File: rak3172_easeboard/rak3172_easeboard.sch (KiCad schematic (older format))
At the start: 49 parts, among them J1 Conn_Coaxial, J2 USB_C_Receptacle_Simply, SW1 SW_Push, SW2 SW_Push, SW3 SW_Push, U1 RAK3172, U2 FT232RL, U3 SPX3819

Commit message: Matching Network
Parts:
- added C8_DNP1: DNP, rak3172_easeboard:C_0805_2012Metric_Pad1.18x1.45mm_HandSolder, symbol rak3172_easeboard:C
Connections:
- net GND: now also C8_DNP1.2
- net at J1.1 (In), R8.1: now also C8_DNP1.1
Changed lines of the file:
@@
 L rak3172_easeboard:GND #PWR03
 U 1 1 61AD1456
-P 1150 6950
-F 0 "#PWR03" H 1150 6700 50  0001 C CNN
-F 1 "GND" H 1155 6777 50  0000 C CNN
-F 2 "" H 1150 6950 50  0001 C CNN
-F 3 "" H 1150 6950 50  0001 C CNN
-	1    1150 6950
-	1    0    0    -1
-$EndComp
-Wire Wire Line
-	1900 6600 1900 6950
-Wire Wire Line
-	1150 6950 1150 6900
+P 1150 7250
+F 0 "#PWR03" H 1150 7000 50  0001 C CNN
+F 1 "GND" H 1155 7077 50  0000 C CNN
+F 2 "" H 1150 7250 50  0001 C CNN
+F 3 "" H 1150 7250 50  0001 C CNN
+	1    1150 7250
+	1    0    0    -1
+$EndComp
 $Comp
 L rak3172_easeboard:VCC #PWR013
@@
 L rak3172_easeboard:GND #PWR04
 U 1 1 6153D503
-P 1900 6950
-F 0 "#PWR04" H 1900 6700 50  0001 C CNN
-F 1 "GND" H 1905 6777 50  0000 C CNN
-F 2 "" H 1900 6950 50  0001 C CNN
-F 3 "" H 1900 6950 50  0001 C CNN
-	1    1900 6950
+P 1900 7250
+F 0 "#PWR04" H 1900 7000 50  0001 C CNN
+F 1 "GND" H 1905 7077 50  0000 C CNN
+F 2 "" H 1900 7250 50  0001 C CNN
+F 3 "" H 1900 7250 50  0001 C CNN
+	1    1900 7250
 	1    0    0    -1
 $EndComp
@@
 	1800 6700 2050 6700
 Wire Wire Line
-	1500 6700 1350 6700
+	1500 6700 1400 6700
 Text Notes 2700 700  0    100  ~ 20
 USB-SERIAL CONVERTER
@@
 Wire Wire Line
 	4500 6000 4650 6000
+$Comp
+L rak3172_easeboard:C C8_DNP1
+U 1 1 61CCCB7A
+P 1400 6950
+F 0 "C8_DNP1" H 1515 6996 50  0000 L CNN
+F 1 "DNP" H 1515 6905 50  0000 L CNN
+F 2 "rak3172_easeboard:C_0805_2012Metric_Pad1.18x1.45mm_HandSolder" H 1350 6450 50  0001 C CNN
+F 3 "https://www.mouser.es/datasheet/2/212/KEM_C1002_X7R_SMD-1102033.pdf" H 1400 6950 50  0001 C CNN
+F 4 "0.09" H 1400 6950 50  0001 C CNN "Last Seen Price (eur)"
+F 5 "https://www.mouser.es/ProductDetail/KEMET/C0805C104M5RACTU?qs=sGAEpiMZZMsh%252B1woXyUXj%252BSRFd9RE8bC9ywBatmv%2F3c%3D" H 1400 6950 50  0001 C CNN "Mouser"
+	1    1400 6950
+	1    0    0    -1
+$EndComp
+$Comp
+L rak3172_easeboard:GND #PWR034
+U 1 1 61CFA2AD
+P 1400 7250
+F 0 "#PWR034" H 1400 7000 50  0001 C CNN
+F 1 "GND" H 1405 7077 50  0000 C CNN
+F 2 "" H 1400 7250 50  0001 C CNN
+F 3 "" H 1400 7250 50  0001 C CNN
+	1    1400 7250
+	1    0    0    -1
+$EndComp
+Wire Wire Line
+	1150 6900 1150 7250
+Wire Wire Line
+	1400 7100 1400 7250
+Wire Wire Line
+	1900 6600 1900 7250
+Wire Wire Line
+	1400 6800 1400 6700
+Connection ~ 1400 6700
+Wire Wire Line
+	1400 6700 1350 6700
 $EndSCHEMATC

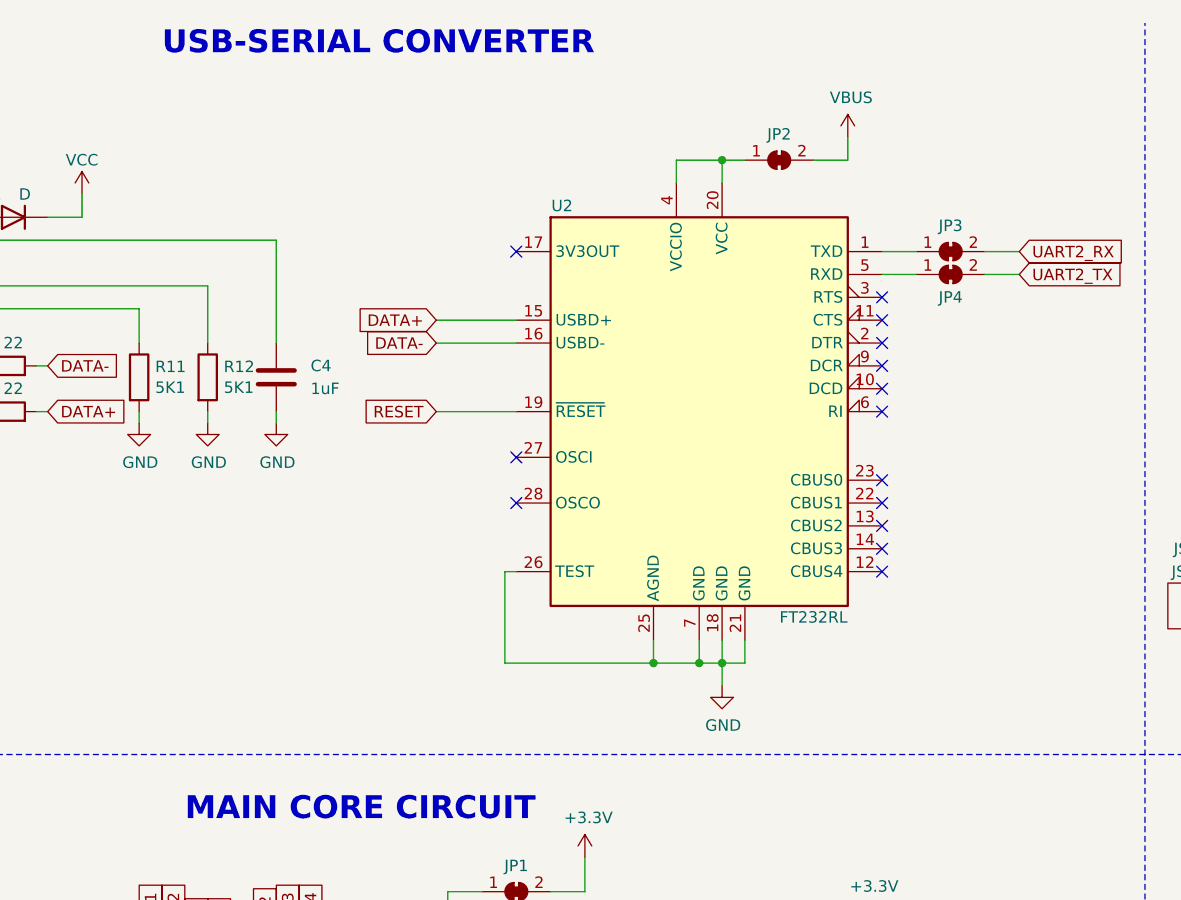
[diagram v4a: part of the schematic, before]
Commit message: Disconnect Reset from usb-serial converter
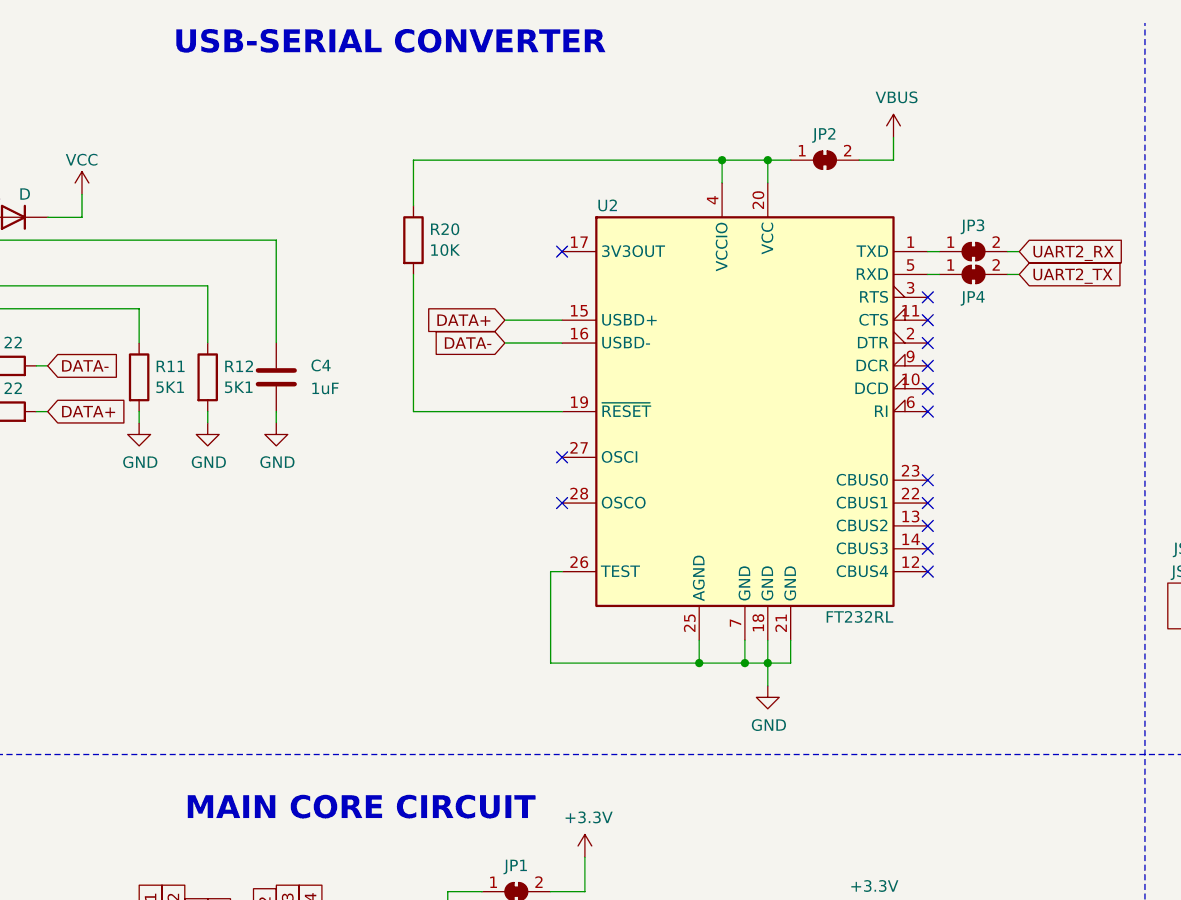
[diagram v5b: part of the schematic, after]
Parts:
- added R20: 10K, rak3172_easeboard:R_0805_2012Metric_Pad1.20x1.40mm_HandSolder, symbol rak3172_easeboard:R
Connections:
- net RESET: no longer U2.19 (~RESET~)
- net at JP2.1 (A), U2.20 (VCC), U2.4 (VCCIO): now also R20.1
- new net: R20.2, U2.19 (~RESET~)
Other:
- moved on the sheet: JP2, JP3, JP4, U2
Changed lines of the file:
@@
 L rak3172_easeboard:GND #PWR010
 U 1 1 61DF3F73
-P 5150 3450
-F 0 "#PWR010" H 5150 3200 50  0001 C CNN
-F 1 "GND" H 5155 3277 50  0000 C CNN
-F 2 "" H 5150 3450 50  0001 C CNN
-F 3 "" H 5150 3450 50  0001 C CNN
-	1    5150 3450
-	1    0    0    -1
-$EndComp
-Wire Wire Line
-	5150 3250 5150 3350
+P 5350 3450
+F 0 "#PWR010" H 5350 3200 50  0001 C CNN
+F 1 "GND" H 5355 3277 50  0000 C CNN
+F 2 "" H 5350 3450 50  0001 C CNN
+F 3 "" H 5350 3450 50  0001 C CNN
+	1    5350 3450
+	1    0    0    -1
+$EndComp
+Wire Wire Line
+	5350 3250 5350 3350
+Wire Wire Line
+	5450 3250 5450 3350
+Wire Wire Line
+	5450 3350 5350 3350
+Connection ~ 5350 3350
+Wire Wire Line
+	5350 3350 5350 3450
 Wire Wire Line
 	5250 3250 5250 3350
 Wire Wire Line
-	5250 3350 5150 3350
-Connection ~ 5150 3350
-Wire Wire Line
-	5150 3350 5150 3450
+	5250 3350 5350 3350
+Text GLabel 4200 1850 0    50   Input ~ 0
+DATA+
+Text GLabel 4200 1950 0    50   Input ~ 0
+DATA-
 Wire Wire Line
 	5050 3250 5050 3350
 Wire Wire Line
-	5050 3350 5150 3350
-Text GLabel 3900 1850 0    50   Input ~ 0
-DATA+
-Text GLabel 3900 1950 0    50   Input ~ 0
-DATA-
-Wire Wire Line
-	3900 1950 4250 1950
-Wire Wire Line
-	4250 1850 3900 1850
-Wire Wire Line
-	4850 3250 4850 3350
-Wire Wire Line
-	4850 3350 5050 3350
+	5050 3350 5250 3350
+Connection ~ 5250 3350
+Wire Wire Line
+	4450 2950 4400 2950
+Wire Wire Line
+	4400 2950 4400 3350
+Wire Wire Line
+	4400 3350 5050 3350
 Connection ~ 5050 3350
-Wire Wire Line
-	4250 2950 4200 2950
-Wire Wire Line
-	4200 2950 4200 3350
-Wire Wire Line
-	4200 3350 4850 3350
-Connection ~ 4850 3350
 $Comp
 L rak3172_easeboard:FT232RL U2
 U 1 1 61DF0F84
-P 5050 2250
-F 0 "U2" H 4450 3150 50  0000 C CNN
-F 1 "FT232RL" H 5550 1350 50  0000 C CNN
-F 2 "rak3172_easeboard:SSOP-28_5.3x10.2mm_P0.65mm" H 6150 1350 50  0001 C CNN
-F 3 "https://www.ftdichip.com/Support/Documents/DataSheets/ICs/DS_FT232R.pdf" H 5050 2250 50  0001 C CNN
-	1    5050 2250
-	1    0    0    -1
-$EndComp
-Wire Wire Line
-	4950 1150 4950 1250
-Wire Wire Line
-	5150 1250 5150 1150
-Connection ~ 5150 1150
-Wire Wire Line
-	5150 1150 4950 1150
-Text GLabel 6450 1550 2    50   Input ~ 0
-UART2_RX
-Text GLabel 6450 1650 2    50   Input ~ 0
-UART2_TX
+P 5250 2250
+F 0 "U2" H 4650 3150 50  0000 C CNN
+F 1 "FT232RL" H 5750 1350 50  0000 C CNN
+F 2 "rak3172_easeboard:SSOP-28_5.3x10.2mm_P0.65mm" H 6350 1350 50  0001 C CNN
+F 3 "https://www.ftdichip.com/Support/Documents/DataSheets/ICs/DS_FT232R.pdf" H 5250 2250 50  0001 C CNN
+	1    5250 2250
+	1    0    0    -1
+$EndComp
+Wire Wire Line
+	5150 1150 5150 1250
+Wire Wire Line
+	5350 1250 5350 1150
+Connection ~ 5350 1150
+Wire Wire Line
+	5350 1150 5150 1150
 Wire Wire Line
 	3150 7250 3150 6950
@@
 Wire Wire Line
 	1500 6700 1400 6700
-Text Notes 2700 700  0    100  ~ 20
+Text Notes 2750 700  0    100  ~ 20
 USB-SERIAL CONVERTER
 $Comp
@@
 Battery Connector
 Wire Wire Line
-	5150 1150 5250 1150
+	5350 1150 5450 1150
 Wire Wire Line
 	3950 4350 4100 4350
@@
 L rak3172_easeboard:SolderJumper_2_Bridged JP2
 U 1 1 61BC7834
-P 5400 1150
-F 0 "JP2" H 5400 1263 50  0000 C CNN
-F 1 "SolderJumper_2_Bridged" H 5400 1050 50  0001 C CNN
-F 2 "rak3172_easeboard:SolderJumper-2_P1.3mm_Bridged_Pad1.0x1.5mm" H 5400 1150 50  0001 C CNN
-F 3 "~" H 5400 1150 50  0001 C CNN
-F 4 "~" H 5400 1150 50  0001 C CNN "Last Seen Price (eur)"
-	1    5400 1150
+P 5600 1150
+F 0 "JP2" H 5600 1263 50  0000 C CNN
+F 1 "SolderJumper_2_Bridged" H 5600 1050 50  0001 C CNN
+F 2 "rak3172_easeboard:SolderJumper-2_P1.3mm_Bridged_Pad1.0x1.5mm" H 5600 1150 50  0001 C CNN
+F 3 "~" H 5600 1150 50  0001 C CNN
+F 4 "~" H 5600 1150 50  0001 C CNN "Last Seen Price (eur)"
+	1    5600 1150
 	1    0    0    -1
 $EndComp
@@
 L rak3172_easeboard:VBUS #PWR025
 U 1 1 6176782E
-P 5700 1050
-F 0 "#PWR025" H 5700 900 50  0001 C CNN
-F 1 "VBUS" H 5715 1223 50  0000 C CNN
-F 2 "" H 5700 1050 50  0001 C CNN
-F 3 "" H 5700 1050 50  0001 C CNN
-	1    5700 1050
-	1    0    0    -1
-$EndComp
-NoConn ~ 5850 2550
-NoConn ~ 5850 2650
-NoConn ~ 5850 2750
-NoConn ~ 5850 2850
-NoConn ~ 5850 2950
-NoConn ~ 5850 2250
-NoConn ~ 5850 2150
-NoConn ~ 4250 2650
-NoConn ~ 4250 2450
-NoConn ~ 5850 2050
-NoConn ~ 5850 1950
-NoConn ~ 5850 1850
-NoConn ~ 5850 1750
-NoConn ~ 4250 1550
-Text GLabel 3900 2250 0    50   Input ~ 0
-RESET
+P 5900 1050
+F 0 "#PWR025" H 5900 900 50  0001 C CNN
+F 1 "VBUS" H 5915 1223 50  0000 C CNN
+F 2 "" H 5900 1050 50  0001 C CNN
+F 3 "" H 5900 1050 50  0001 C CNN
+	1    5900 1050
+	1    0    0    -1
+$EndComp
+NoConn ~ 6050 2550
+NoConn ~ 6050 2650
+NoConn ~ 6050 2750
+NoConn ~ 6050 2850
+NoConn ~ 6050 2950
+NoConn ~ 6050 2250
+NoConn ~ 6050 2150
+NoConn ~ 4450 2650
+NoConn ~ 4450 2450
+NoConn ~ 6050 2050
+NoConn ~ 6050 1950
+NoConn ~ 6050 1850
+NoConn ~ 6050 1750
+NoConn ~ 4450 1550
 $Comp
 L rak3172_easeboard:R R2
@@
 $EndComp
 Wire Wire Line
-	4250 2250 3900 2250
-Wire Wire Line
 	8900 2000 8900 2050
 Wire Wire Line
@@
 	8200 2900 8200 2950
 Wire Wire Line
-	5700 1050 5700 1150
-Wire Wire Line
-	5700 1150 5550 1150
+	5900 1050 5900 1150
+Wire Wire Line
+	5900 1150 5750 1150
 Wire Wire Line
 	850  4950 1050 4950
@@
 $EndComp
 Wire Wire Line
-	6300 1650 6450 1650
-Wire Wire Line
-	5850 1650 6000 1650
-Wire Wire Line
-	6300 1550 6450 1550
-Wire Wire Line
-	5850 1550 6000 1550
-$Comp
-L rak3172_easeboard:SolderJumper_2_Bridged JP4
-U 1 1 61BC86E2
-P 6150 1650
-F 0 "JP4" H 6150 1550 50  0000 C CNN
-F 1 "SolderJumper_2_Bridged" H 6150 1550 50  0001 C CNN
-F 2 "rak3172_easeboard:SolderJumper-2_P1.3mm_Bridged_Pad1.0x1.5mm" H 6150 1650 50  0001 C CNN
-F 3 "~" H 6150 1650 50  0001 C CNN
-F 4 "~" H 6150 1650 50  0001 C CNN "Last Seen Price (eur)"
-	1    6150 1650
-	1    0    0    -1
-$EndComp
-$Comp
-L rak3172_easeboard:SolderJumper_2_Bridged JP3
-U 1 1 61BC80B7
-P 6150 1550
-F 0 "JP3" H 6150 1663 50  0000 C CNN
-F 1 "SolderJumper_2_Bridged" H 6150 1450 50  0001 C CNN
-F 2 "rak3172_easeboard:SolderJumper-2_P1.3mm_Bridged_Pad1.0x1.5mm" H 6150 1550 50  0001 C CNN
-F 3 "~" H 6150 1550 50  0001 C CNN
-F 4 "~" H 6150 1550 50  0001 C CNN "Last Seen Price (eur)"
-	1    6150 1550
-	1    0    0    -1
-$EndComp
-Wire Wire Line
 	1750 5000 1750 4950
 Wire Wire Line
@@
 Wire Wire Line
 	1400 6700 1350 6700
+$Comp
+L rak3172_easeboard:R R20
+U 1 1 627371A7
+P 3800 1500
+F 0 "R20" H 3870 1546 50  0000 L CNN
+F 1 "10K" H 3870 1455 50  0000 L CNN
+F 2 "rak3172_easeboard:R_0805_2012Metric_Pad1.20x1.40mm_HandSolder" V 3730 1500 50  0001 C CNN
+F 3 "https://www.mouser.es/datasheet/2/392/susumu_RR_Data_Sheet-1206438.pdf" H 3800 1500 50  0001 C CNN
+F 4 "0.09" H 3800 1500 50  0001 C CNN "Last Seen Price (eur)"
+F 5 "https://www.mouser.es/ProductDetail/Susumu/RR1220P-103-D?qs=nCAm%252BcMdy9wM6YRNq%2FvwoQ%3D%3D" H 3800 1500 50  0001 C CNN "Mouser"
+	1    3800 1500
+	1    0    0    -1
+$EndComp
+$Comp
+L rak3172_easeboard:SolderJumper_2_Bridged JP3
+U 1 1 61BC80B7
+P 6250 1550
+F 0 "JP3" H 6250 1663 50  0000 C CNN
+F 1 "SolderJumper_2_Bridged" H 6250 1450 50  0001 C CNN
+F 2 "rak3172_easeboard:SolderJumper-2_P1.3mm_Bridged_Pad1.0x1.5mm" H 6250 1550 50  0001 C CNN
+F 3 "~" H 6250 1550 50  0001 C CNN
+F 4 "~" H 6250 1550 50  0001 C CNN "Last Seen Price (eur)"
+	1    6250 1550
+	1    0    0    -1
+$EndComp
+$Comp
+L rak3172_easeboard:SolderJumper_2_Bridged JP4
+U 1 1 61BC86E2
+P 6250 1650
+F 0 "JP4" H 6250 1550 50  0000 C CNN
+F 1 "SolderJumper_2_Bridged" H 6250 1550 50  0001 C CNN
+F 2 "rak3172_easeboard:SolderJumper-2_P1.3mm_Bridged_Pad1.0x1.5mm" H 6250 1650 50  0001 C CNN
+F 3 "~" H 6250 1650 50  0001 C CNN
+F 4 "~" H 6250 1650 50  0001 C CNN "Last Seen Price (eur)"
+	1    6250 1650
+	1    0    0    -1
+$EndComp
+Text GLabel 6450 1650 2    50   Input ~ 0
+UART2_TX
+Text GLabel 6450 1550 2    50   Input ~ 0
+UART2_RX
+Wire Wire Line
+	6100 1550 6050 1550
+Wire Wire Line
+	6050 1650 6100 1650
+Wire Wire Line
+	6400 1550 6450 1550
+Wire Wire Line
+	6400 1650 6450 1650
+Wire Wire Line
+	4200 1850 4450 1850
+Wire Wire Line
+	4450 1950 4200 1950
+Wire Wire Line
+	3800 2250 3800 1650
+Wire Wire Line
+	3800 2250 4450 2250
+Wire Wire Line
+	5150 1150 3800 1150
+Wire Wire Line
+	3800 1150 3800 1350
+Connection ~ 5150 1150
 $EndSCHEMATC
